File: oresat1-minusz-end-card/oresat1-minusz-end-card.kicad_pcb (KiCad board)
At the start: 4 copper layers, 99.8 x 94.6 mm, 90 parts, among them J1 J-SAMTEC-TFM-120-01-L-D-RA, J2 U.FL-R-SMT-1, J3 M55-7101242R, J5 M55-7101242R, Q1 DMP2240UDM, Q2 PMV45EN, Q3 PMV45EN, Q4 PMV45EN, Q5 DMP2240UDM-7, Q6 PMV45EN, Q7 DMP2240UDM-7, U11 MIC842LYC5, U12 MIC842LYC5, U2 MAX7310, U201 TS5A21366, U202 TS5A21366, U203 TS5A21366, U204 TS5A21366

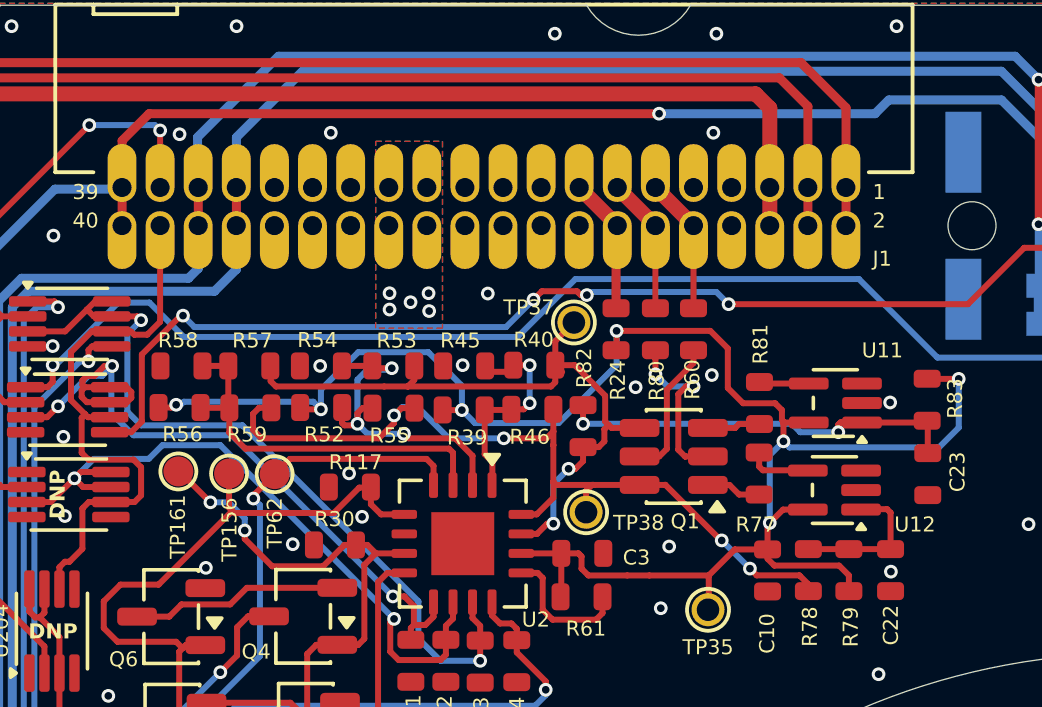
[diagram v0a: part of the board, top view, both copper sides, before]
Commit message: FIxed OPD connection
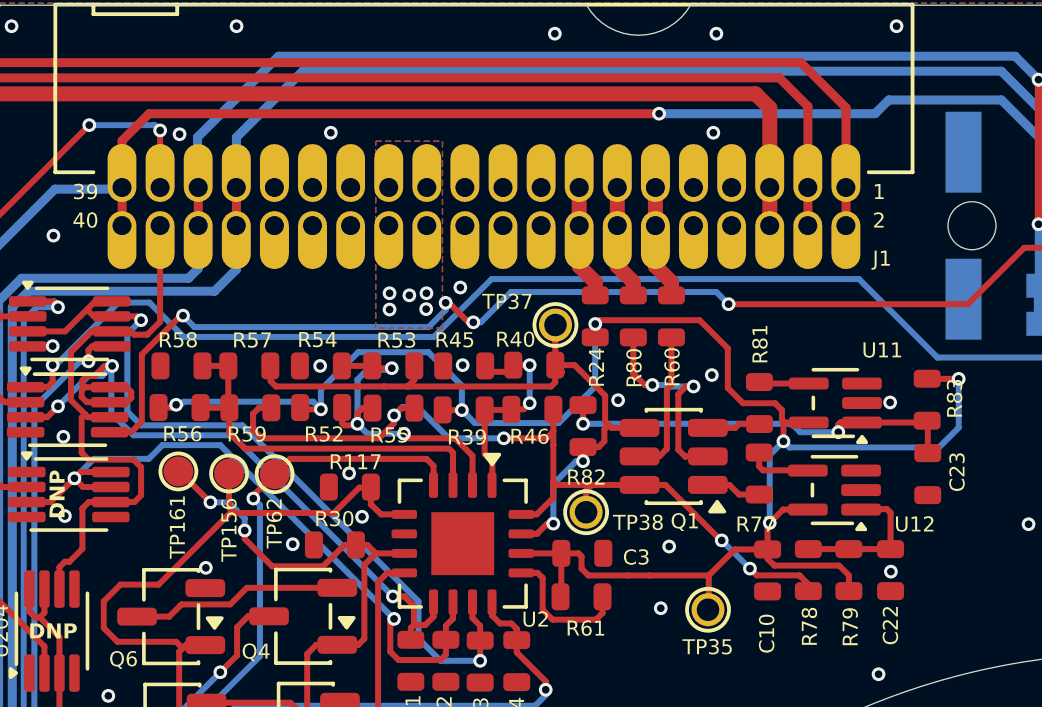
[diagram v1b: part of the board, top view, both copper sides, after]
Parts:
- moved R60 0.85 mm to (133.1, 68.1)
- moved R80 0.85 mm to (131.8, 68.1)
- moved R24 0.82 mm to (130.6, 68.1)
- moved TP37 0.62 mm to (129.2, 68.4)
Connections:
- J1 pad 10: /OPD_SDA -> unconnected-(J1-Pad10)
- J1 pad 12: /OPD_SCL -> /OPD_SDA
- J1 pad 14: /OPD_PWR -> /OPD_SCL
- J1 pad 16: unconnected-(J1-Pad16) -> /OPD_PWR
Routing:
- net Net-(Q1B-S): track 5.79 -> 6.94 mm
- net /OPD_PWR: track 4.57 -> 3.82 mm
- net /OPD_SDA: track 4.55 -> 3.82 mm
- net /OPD_SCL: track 4.55 -> 3.82 mm
- net VPD: track 61.0 -> 61.6 mm
- net /PX_UART_TX: track 39.2 -> 39.8 mm
